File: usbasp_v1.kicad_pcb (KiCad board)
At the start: 2 copper layers, 21 parts, among them J1 2x5 Box Conn, J2 USB_B, U1 ATmega328-PU, Y1 12MHz

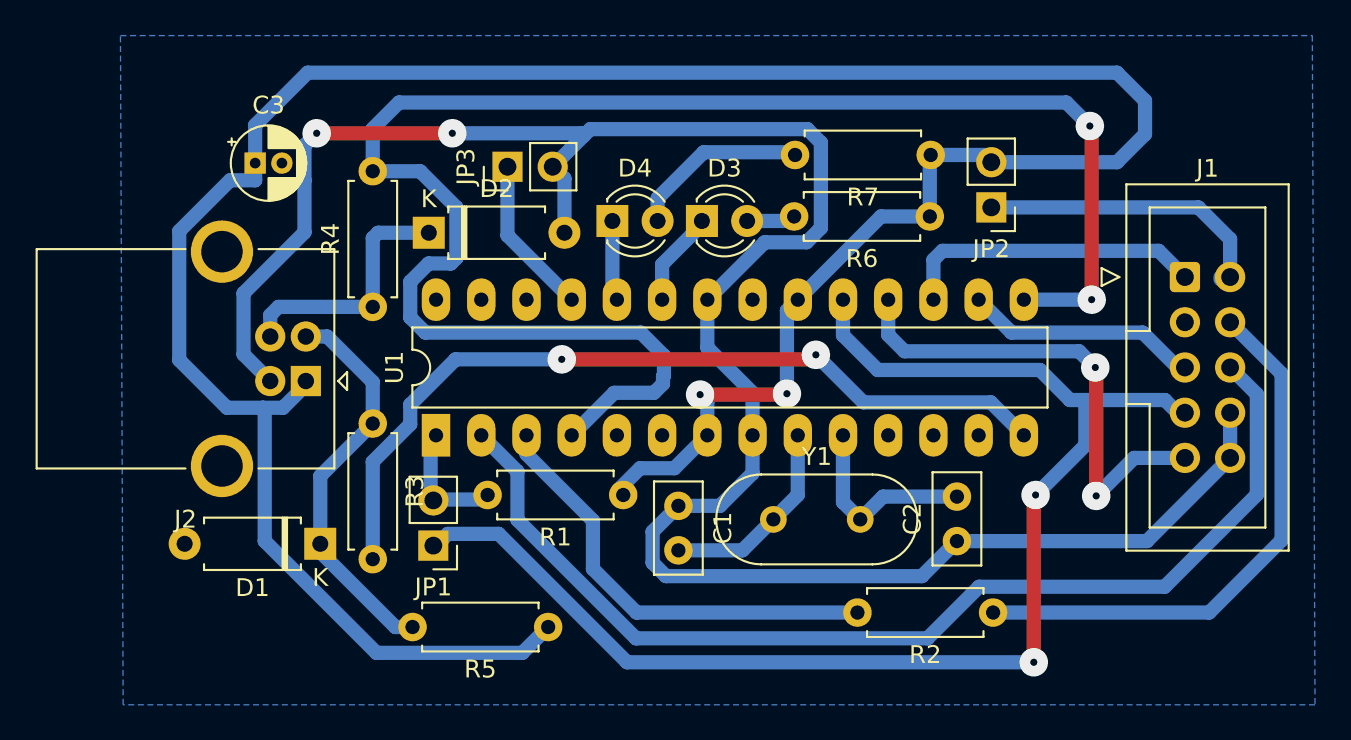
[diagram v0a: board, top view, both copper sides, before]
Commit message: Increased pad sizes for better toner transfer
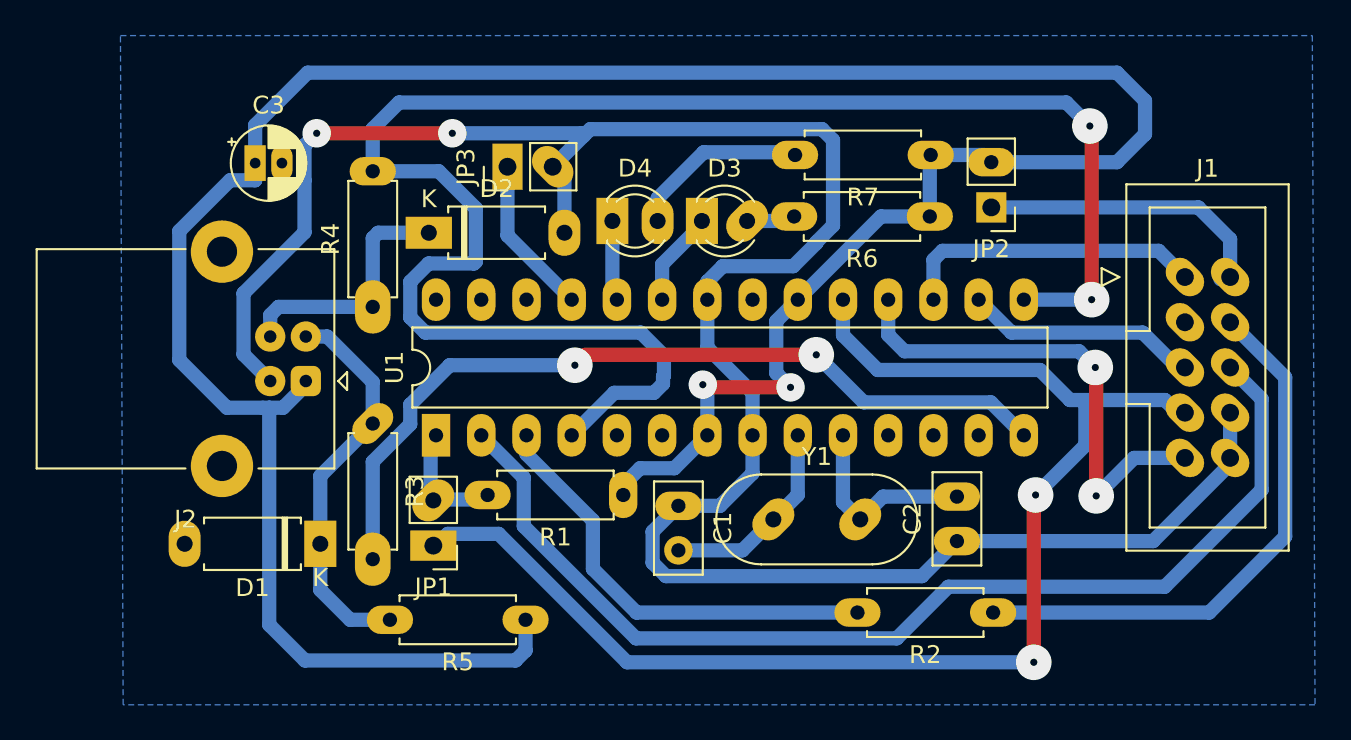
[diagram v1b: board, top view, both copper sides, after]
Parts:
- moved R5 1.33 mm to (129.1, 103.7)
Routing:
- net +5V: track 150.5 -> 154.0 mm
- net Net-(R4-Pad2): track 94.0 -> 96.3 mm
- net GND: track 122.0 -> 124.2 mm

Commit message: Corrected ground plane connection
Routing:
- net GND: track 124.2 -> 138.4 mm, vias 2 -> 4
